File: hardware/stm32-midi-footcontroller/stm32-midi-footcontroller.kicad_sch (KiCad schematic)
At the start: 0 parts

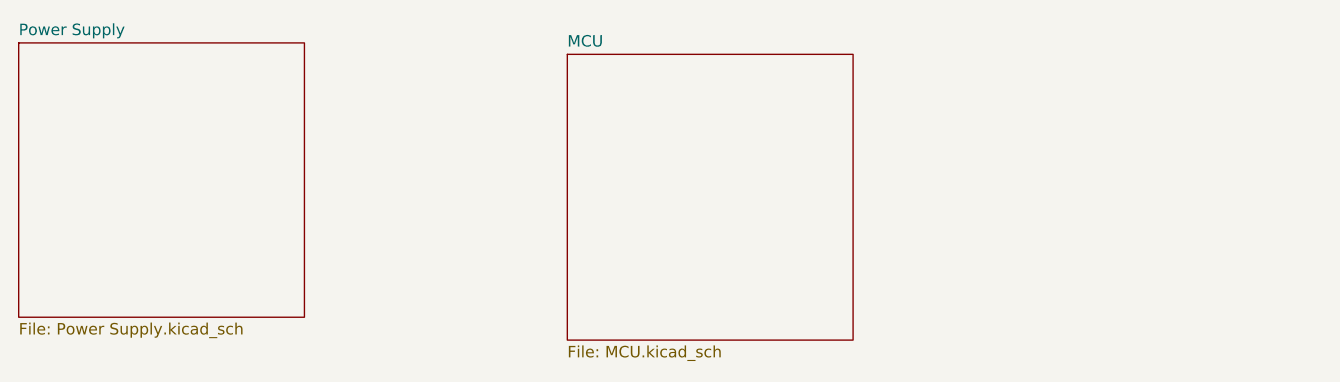
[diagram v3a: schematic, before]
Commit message: add midi hardware to schematic
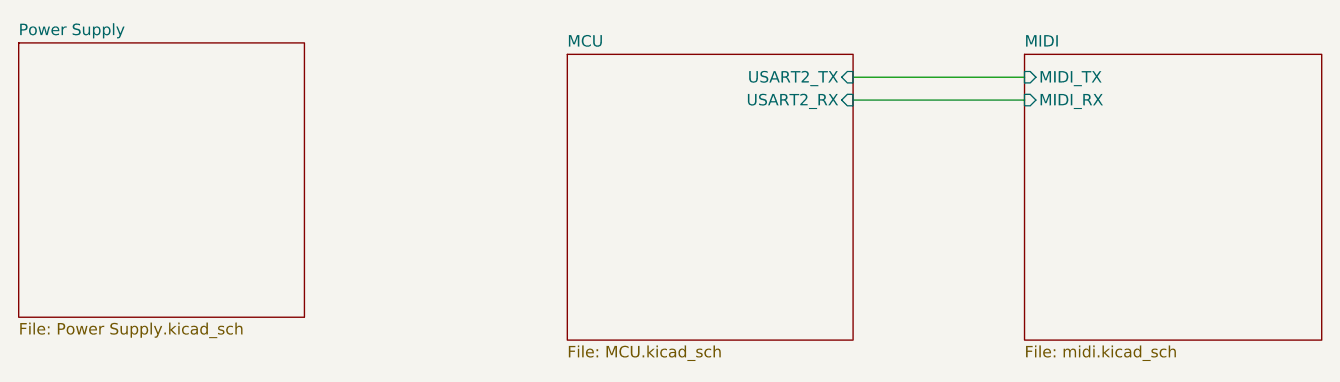
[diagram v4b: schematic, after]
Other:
- added sheet MIDI (midi.kicad_sch)
- sheet MCU ports: added USART2_RX, USART2_TX; removed none
